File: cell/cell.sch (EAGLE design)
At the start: 11 parts

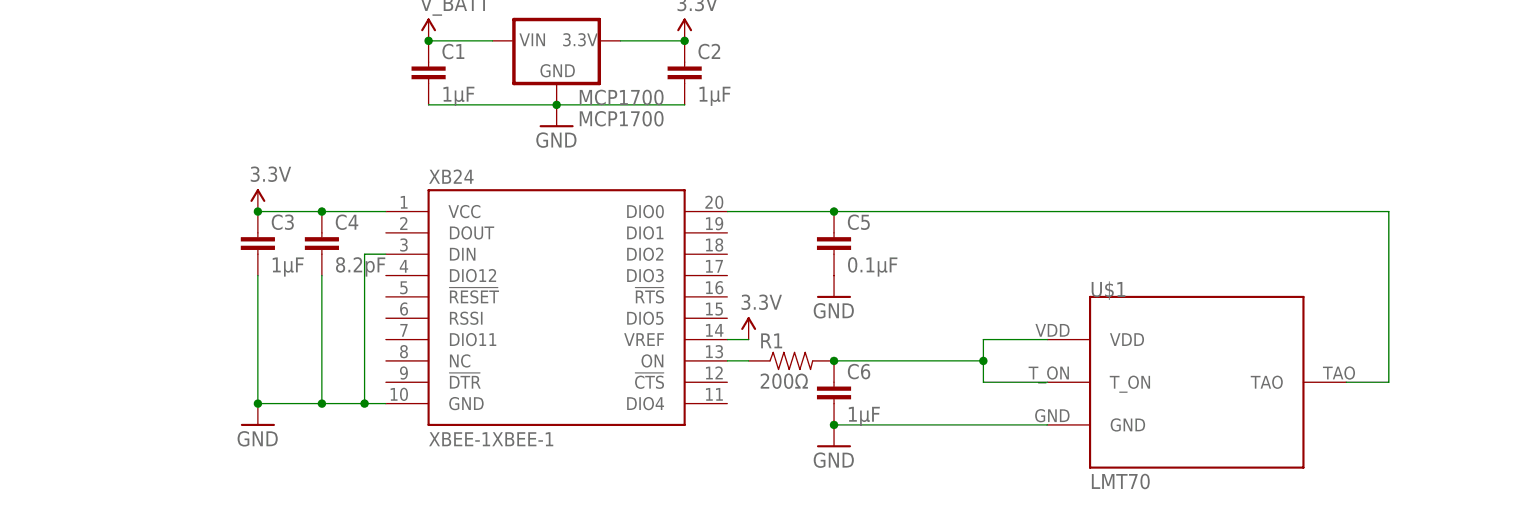
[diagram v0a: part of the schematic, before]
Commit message: Doodles from @raphaelabrams - simplified the power supply rail to a star - strengthened the ground plane - added several decoupling capacitors
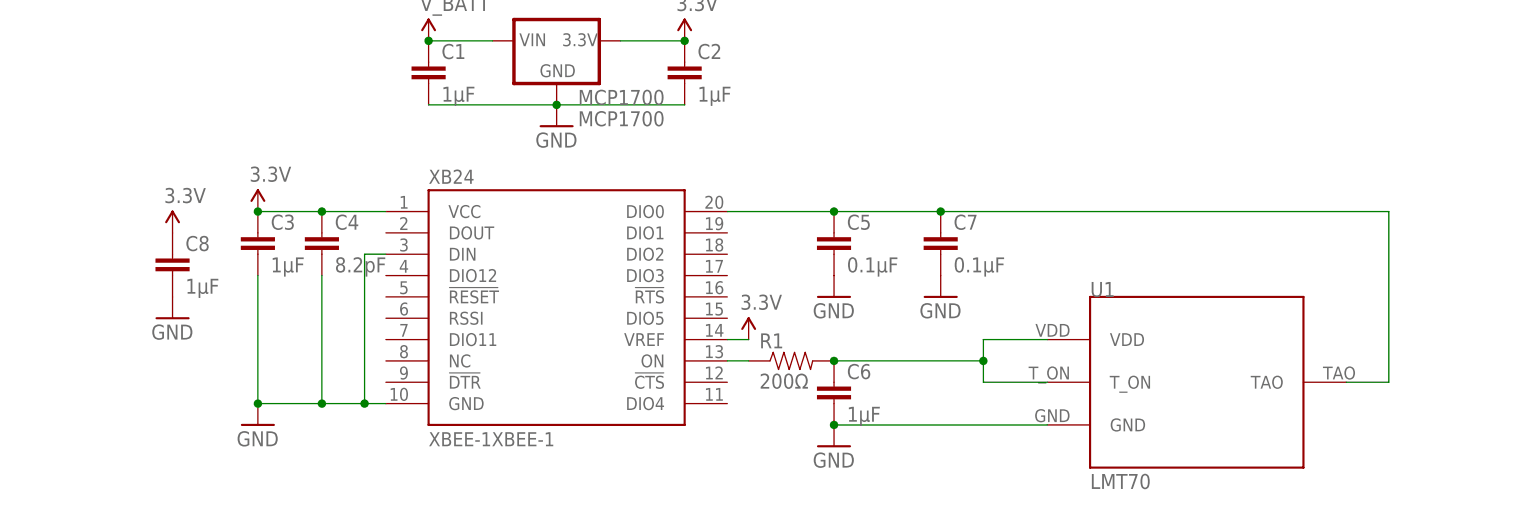
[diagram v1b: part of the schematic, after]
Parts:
- added C7: 0.1µF, SparkFun-Capacitors:CAP0805
- added C8: 1µF, SparkFun-Capacitors:CAP0805
- renumbered U$1 to U1
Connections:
- net 3.3V: now also C8.1
- net GND: now also C7.2, C8.2
- net N$7: now also C7.1
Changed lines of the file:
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@@
 <part name="C2" library="SparkFun-Capacitors" deviceset="CAP" device="0805" value="1µF"/>
 <part name="XB24" library="hrldcpr" deviceset="XBEE-1" device="XBEE-1"/>
-<part name="U$1" library="lmt70" deviceset="LMT70" device=""/>
+<part name="U1" library="lmt70" deviceset="LMT70" device=""/>
+<part name="C7" library="SparkFun-Capacitors" deviceset="CAP" device="0805" value="0.1µF"/>
+<part name="GND5" library="SparkFun-Aesthetics" deviceset="GND" device=""/>
+<part name="SUPPLY5" library="SparkFun-Aesthetics" deviceset="3.3V" device=""/>
+<part name="C8" library="SparkFun-Capacitors" deviceset="CAP" device="0805" value="1µF"/>
+<part name="GND6" library="SparkFun-Aesthetics" deviceset="GND" device=""/>
 </parts>
 <sheets>
@@
 <instance part="C2" gate="G$1" x="119.38" y="114.3"/>
 <instance part="XB24" gate="G$1" x="104.14" y="88.9"/>
-<instance part="U$1" gate="G$1" x="180.34" y="78.74"/>
+<instance part="U1" gate="G$1" x="180.34" y="78.74"/>
+<instance part="C7" gate="G$1" x="149.86" y="93.98"/>
+<instance part="GND5" gate="1" x="149.86" y="88.9"/>
+<instance part="SUPPLY5" gate="G$1" x="58.42" y="96.52"/>
+<instance part="C8" gate="G$1" x="58.42" y="91.44"/>
+<instance part="GND6" gate="1" x="58.42" y="86.36"/>
 </instances>
 <busses>
@@
 <pinref part="C6" gate="G$1" pin="2"/>
 <junction x="137.16" y="73.66"/>
-<pinref part="U$1" gate="G$1" pin="GND"/>
+<pinref part="U1" gate="G$1" pin="GND"/>
 <wire x1="137.16" y1="73.66" x2="162.56" y2="73.66" width="0.1524" layer="91"/>
 </segment>
@@
 <wire x1="81.28" y1="93.98" x2="81.28" y2="76.2" width="0.1524" layer="91"/>
 <junction x="81.28" y="76.2"/>
+</segment>
+<segment>
+<pinref part="C7" gate="G$1" pin="2"/>
+<pinref part="GND5" gate="1" pin="GND"/>
+</segment>
+<segment>
+<pinref part="C8" gate="G$1" pin="2"/>
+<pinref part="GND6" gate="1" pin="GND"/>
 </segment>
 </net>
@@
 <junction x="119.38" y="119.38"/>
 </segment>
+<segment>
+<pinref part="SUPPLY5" gate="G$1" pin="3.3V"/>
+<pinref part="C8" gate="G$1" pin="1"/>
+</segment>
 </net>
 <net name="V_BATT" class="0">
@@
 <wire x1="137.16" y1="81.28" x2="154.94" y2="81.28" width="0.1524" layer="91"/>
 <wire x1="154.94" y1="81.28" x2="154.94" y2="83.82" width="0.1524" layer="91"/>
-<pinref part="U$1" gate="G$1" pin="VDD"/>
+<pinref part="U1" gate="G$1" pin="VDD"/>
 <wire x1="154.94" y1="83.82" x2="162.56" y2="83.82" width="0.1524" layer="91"/>
-<pinref part="U$1" gate="G$1" pin="T_ON"/>
+<pinref part="U1" gate="G$1" pin="T_ON"/>
 <wire x1="162.56" y1="78.74" x2="154.94" y2="78.74" width="0.1524" layer="91"/>
 <wire x1="154.94" y1="78.74" x2="154.94" y2="81.28" width="0.1524" layer="91"/>
@@
 <wire x1="137.16" y1="99.06" x2="124.46" y2="99.06" width="0.1524" layer="91"/>
 <pinref part="XB24" gate="G$1" pin="DIO0"/>
-<pinref part="U$1" gate="G$1" pin="TAO"/>
+<pinref part="U1" gate="G$1" pin="TAO"/>
 <wire x1="198.12" y1="78.74" x2="203.2" y2="78.74" width="0.1524" layer="91"/>
 <wire x1="203.2" y1="78.74" x2="203.2" y2="99.06" width="0.1524" layer="91"/>
-<wire x1="137.16" y1="99.06" x2="203.2" y2="99.06" width="0.1524" layer="91"/>
+<wire x1="137.16" y1="99.06" x2="149.86" y2="99.06" width="0.1524" layer="91"/>
 <junction x="137.16" y="99.06"/>
+<pinref part="C7" gate="G$1" pin="1"/>
+<wire x1="149.86" y1="99.06" x2="203.2" y2="99.06" width="0.1524" layer="91"/>
+<junction x="149.86" y="99.06"/>
 </segment>
 </net>
